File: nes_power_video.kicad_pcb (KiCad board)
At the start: 2 copper layers, 59.9 x 59.7 mm, 23 parts, among them J2 Audio, J3 Video, J4 Conn_01x05, J5 RGB conn feed, Q1 2SA733, U1 TPS2553DBV

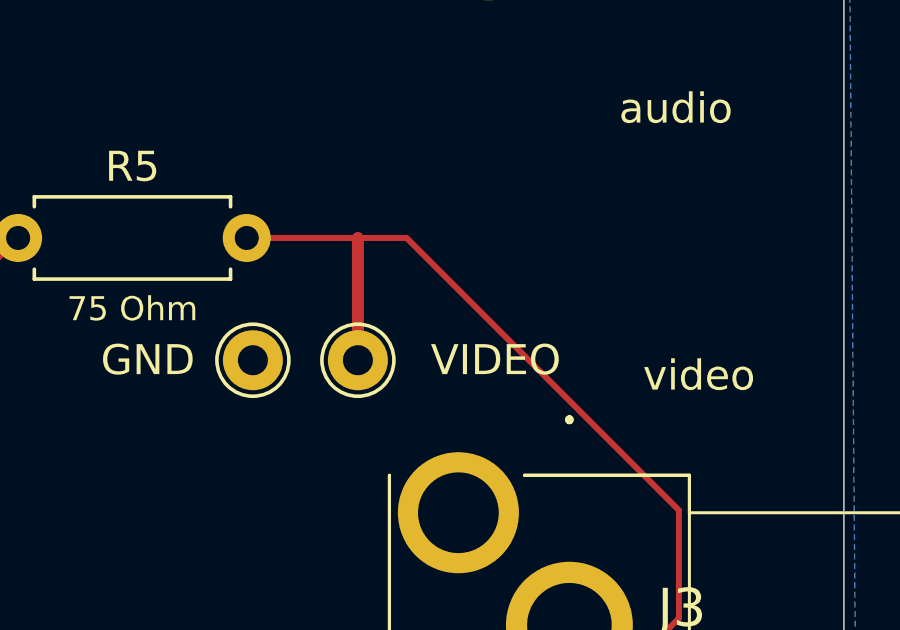
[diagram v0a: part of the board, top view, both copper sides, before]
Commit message: Clear both pre-fab gate blockers: J5's library prefix and TP1's courtyard
The gate refuses to export while either of these stands.

J5 was added in a08b93d with a bare footprint identifier,
"PinHeader_1x03_P2.54mm_Vertical", while its symbol asks for
"Connector_PinHeader_2.54mm:PinHeader_1x03_P2.54mm_Vertical". The pads on
the board are identical to the library part, so only the string was wrong.

TP1's 1.5mm courtyard sat 0.935mm from the corner of J3's, overlapping it
by 0.565mm. TP2 fixes a 3mm minimum to TP1's left and J3 blocks right and
below, so TP1 moves 1mm up to (62, 59) and the VIDEO_OUT track start
follows it. This breaks the TP1/TP2 row alignment, which was cosmetic.

Zone fills are refreshed by the gate's --refill-zones pass.

check_nets.py still passes every invariant -- TP1.1 remains on VIDEO_OUT
alongside R5.2 and J3.2, and SCH vs PCB nets are identical -- and the gate
now exits 0 with the same 33 cosmetic findings as before.

Co-Authored-By: Claude Opus 5 <noreply@anthropic.com>
Claude-Session: https://claude.ai/code/session_015cBpXXsa64nHGznWVANbeU
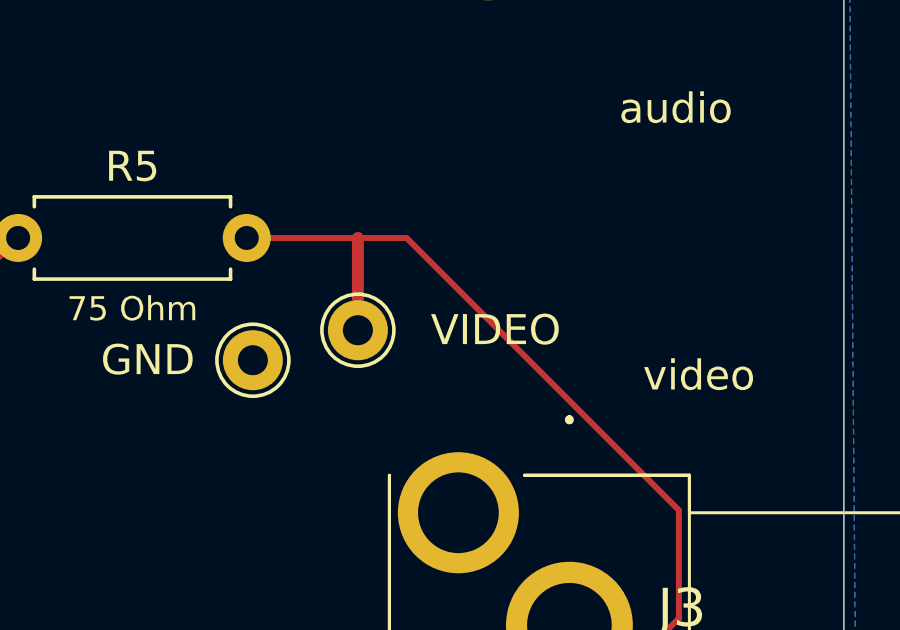
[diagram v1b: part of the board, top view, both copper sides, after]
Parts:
- J5: footprint PinHeader_1x03_P2.54mm_Vertical -> Connector_PinHeader_2.54mm:PinHeader_1x03_P2.54mm_Vertical
- moved TP1 1.00 mm to (62.0, 59.0)
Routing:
- net /VIDEO_OUT: track 34.8 -> 33.8 mm
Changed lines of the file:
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@@
 	(footprint "TestPoint:TestPoint_THTPad_D2.0mm_Drill1.0mm"
 		(layer "F.Cu")
-		(at 62 60)
+		(at 62 59)
 		(descr "THT pad as test Point, diameter 2.0mm, hole diameter 1.0mm")
 		(tags "test point THT pad")
@@
 		)
 	)
-	(footprint "PinHeader_1x03_P2.54mm_Vertical"
+	(footprint "Connector_PinHeader_2.54mm:PinHeader_1x03_P2.54mm_Vertical"
 		(layer "F.Cu")
 		(at 38 74 90)
@@
 	)
 	(segment
-		(start 62 60)
+		(start 62 59)
 		(end 62 55.925)
 		(width 0.4)
